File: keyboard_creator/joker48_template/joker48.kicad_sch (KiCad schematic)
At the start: 20 parts, among them U1 BL24C256A-SFRC, U2 STM32F411CEU6, X1 ARM JTAG, Y1 7325-0800A2010-00

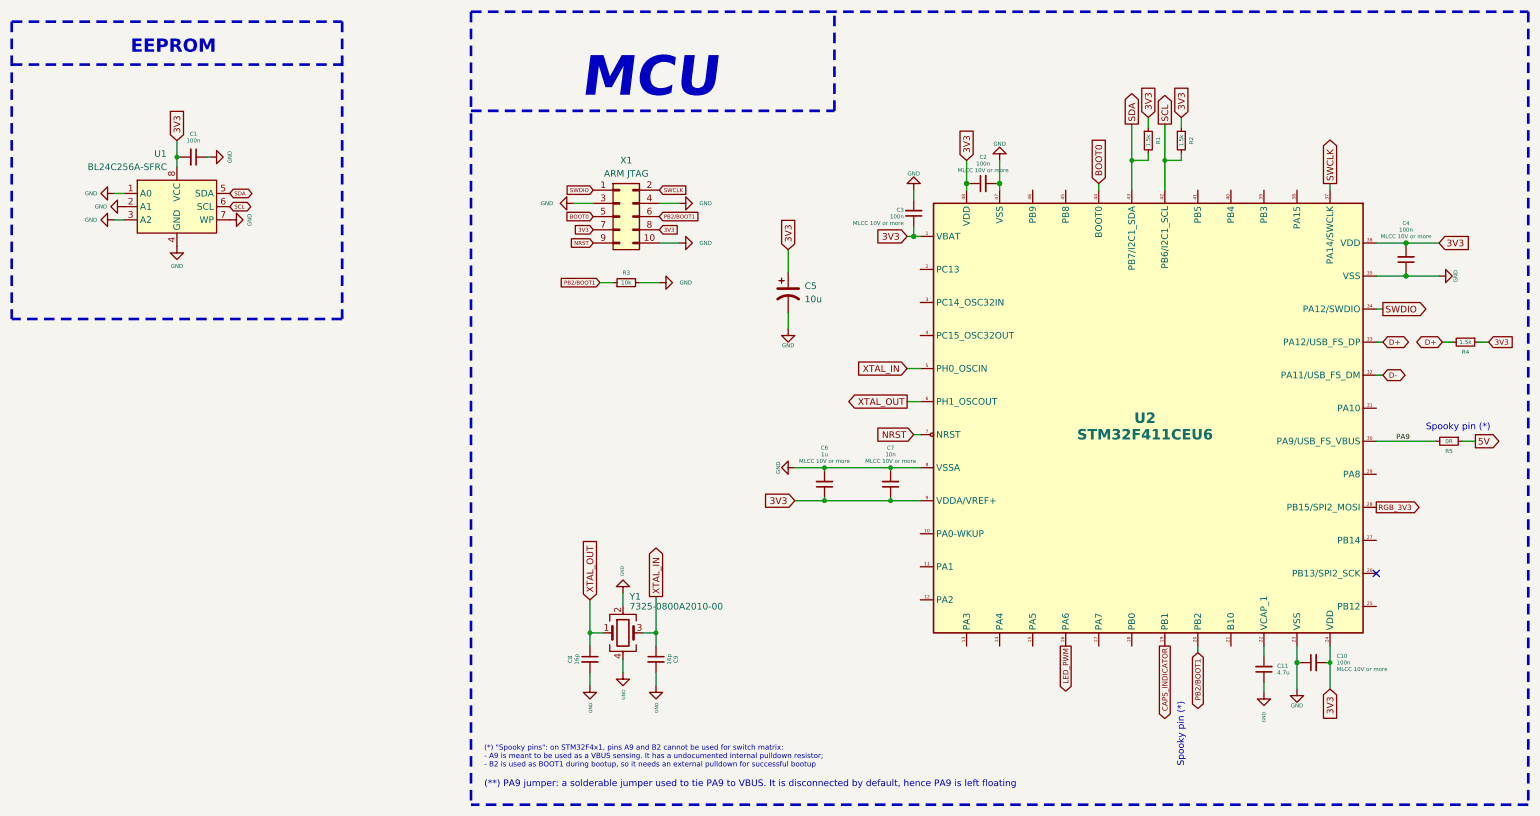
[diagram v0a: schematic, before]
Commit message: Update J48 metadata
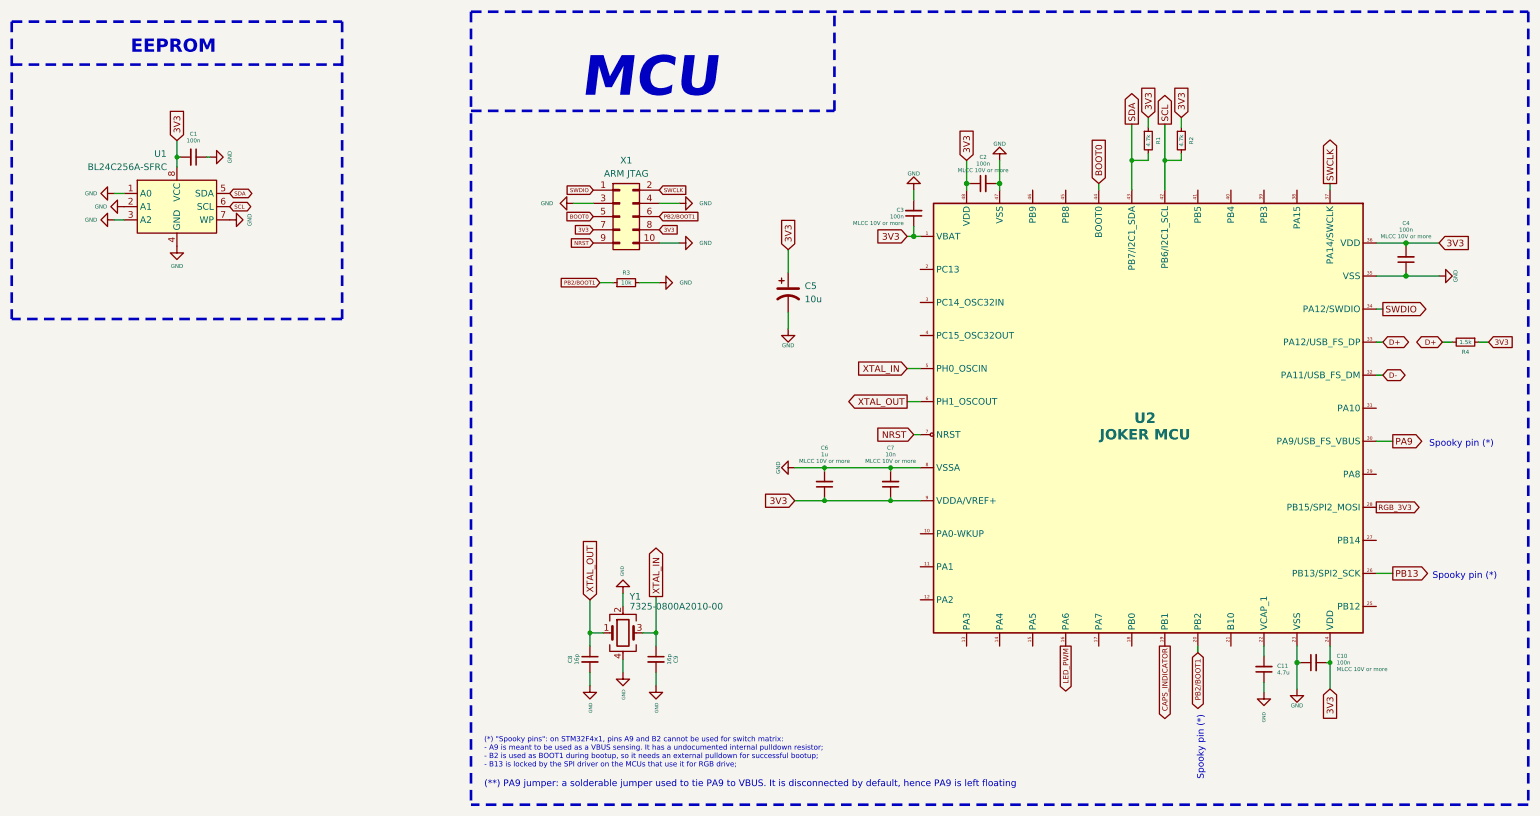
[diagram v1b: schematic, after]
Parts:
- removed R5: 0R, Resistor_SMD:R_0805_2012Metric, symbol Device:R_Small
- R1, R2: value 1.5k -> 4.7k
- U2: value STM32F411CEU6 -> JOKER MCU; Manufacturer STMicroelectronics -> (none); Manufacturer Part Number STM32F411 -> (none); Package UFQFPN-48 -> (none); Vendor Part Number LCSC C60420 (https://lcsc.com/product-detail/ST-Microelectr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 -> (none)
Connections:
- net PB13: now reaches U2.26 (PB13)
- no-connect marks 1 -> 0
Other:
- note added: "(*) "Spooky pins": on STM32F4x1, pins A9 and B2 cannot be used for switch matrix: - A9 is meant to be used as a VBUS sensing. It has a undocumented internal pulldown resistor; - B2 is used as BOOT1 during bootup, so it needs an external pulldown for successful bootup; - B13 is locked by the SPI driver on the MCUs that use it for RGB drive;"
- note removed: "(*) "Spooky pins": on STM32F4x1, pins A9 and B2 cannot be used for switch matrix: - A9 is meant to be used as a VBUS sensing. It has a undocumented internal pulldown resistor; - B2 is used as BOOT1 during bootup, so it needs an external pulldown for successful bootup"
- title: Noxary X60 -> Acheron Joker48 template schematic
